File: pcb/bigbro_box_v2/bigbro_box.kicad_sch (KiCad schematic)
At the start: 42 parts, among them J1 Current Sense, J2 Display, J3 Mains, J4 Debug, J5 RFID, J6 Relay, J7 Ext, K1 G5LE-1, Q1 MMBT3904, Q2 MMBT3904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

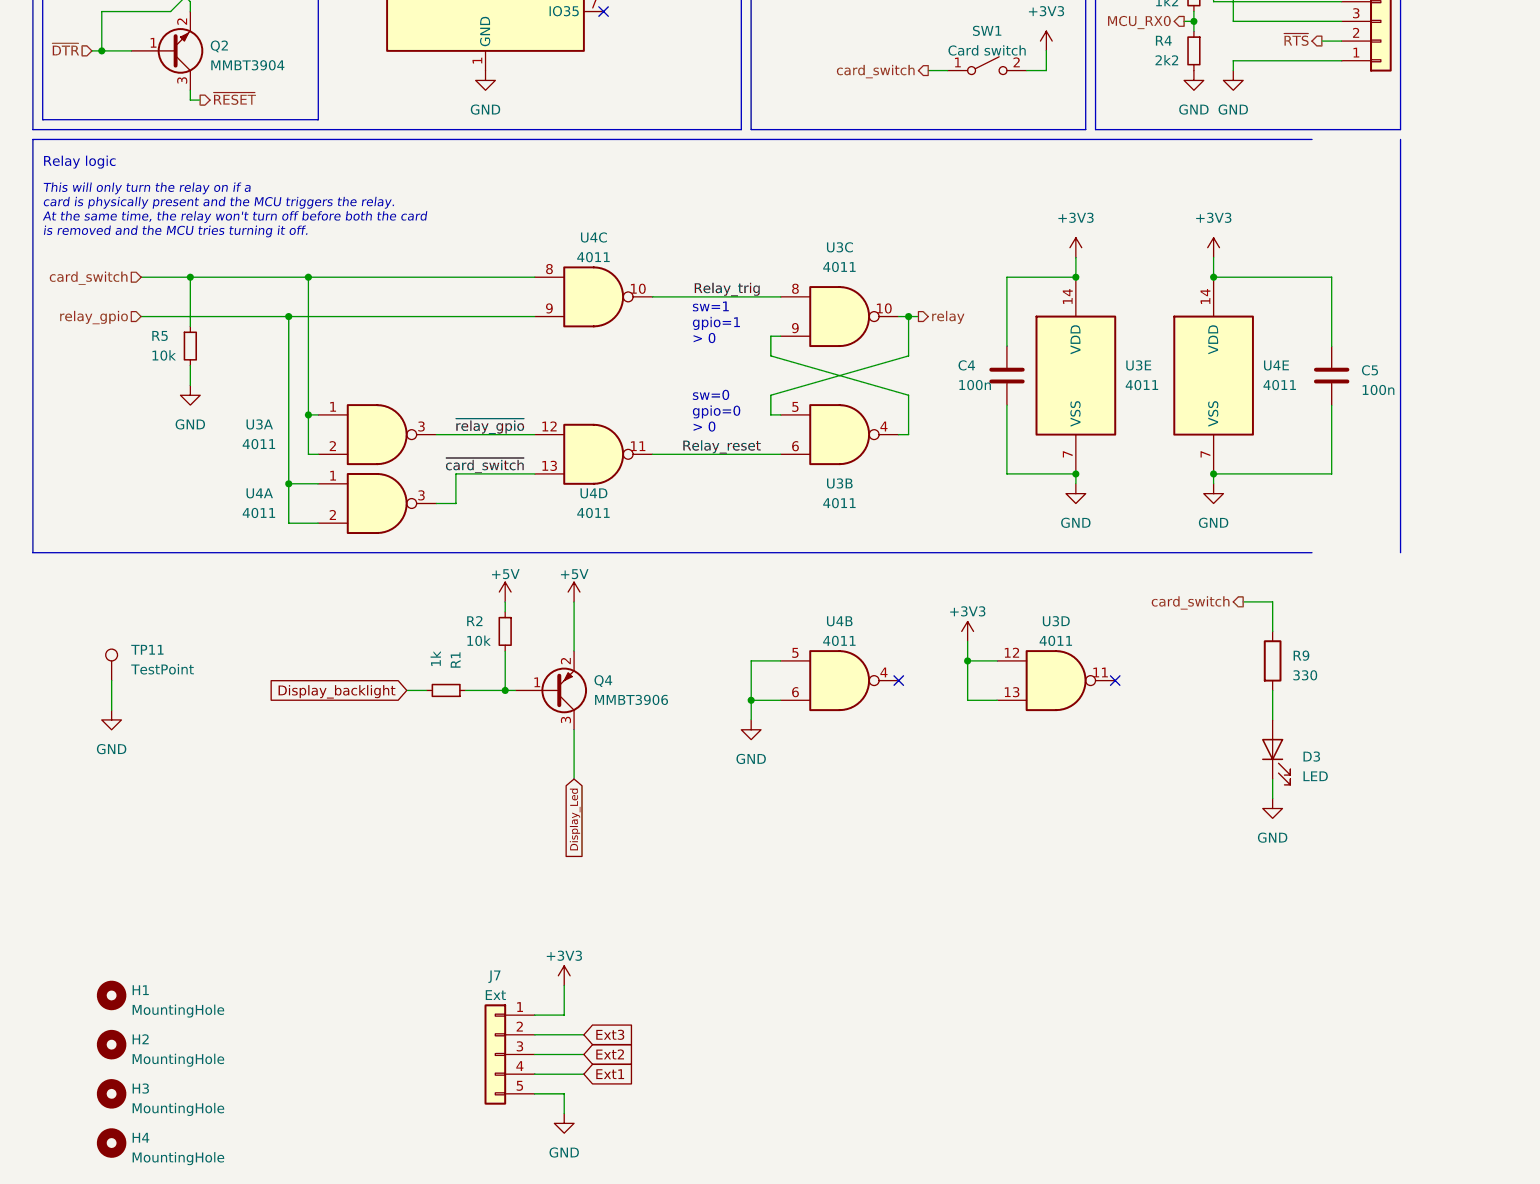
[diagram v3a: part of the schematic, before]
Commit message: Add reset and boot switches.
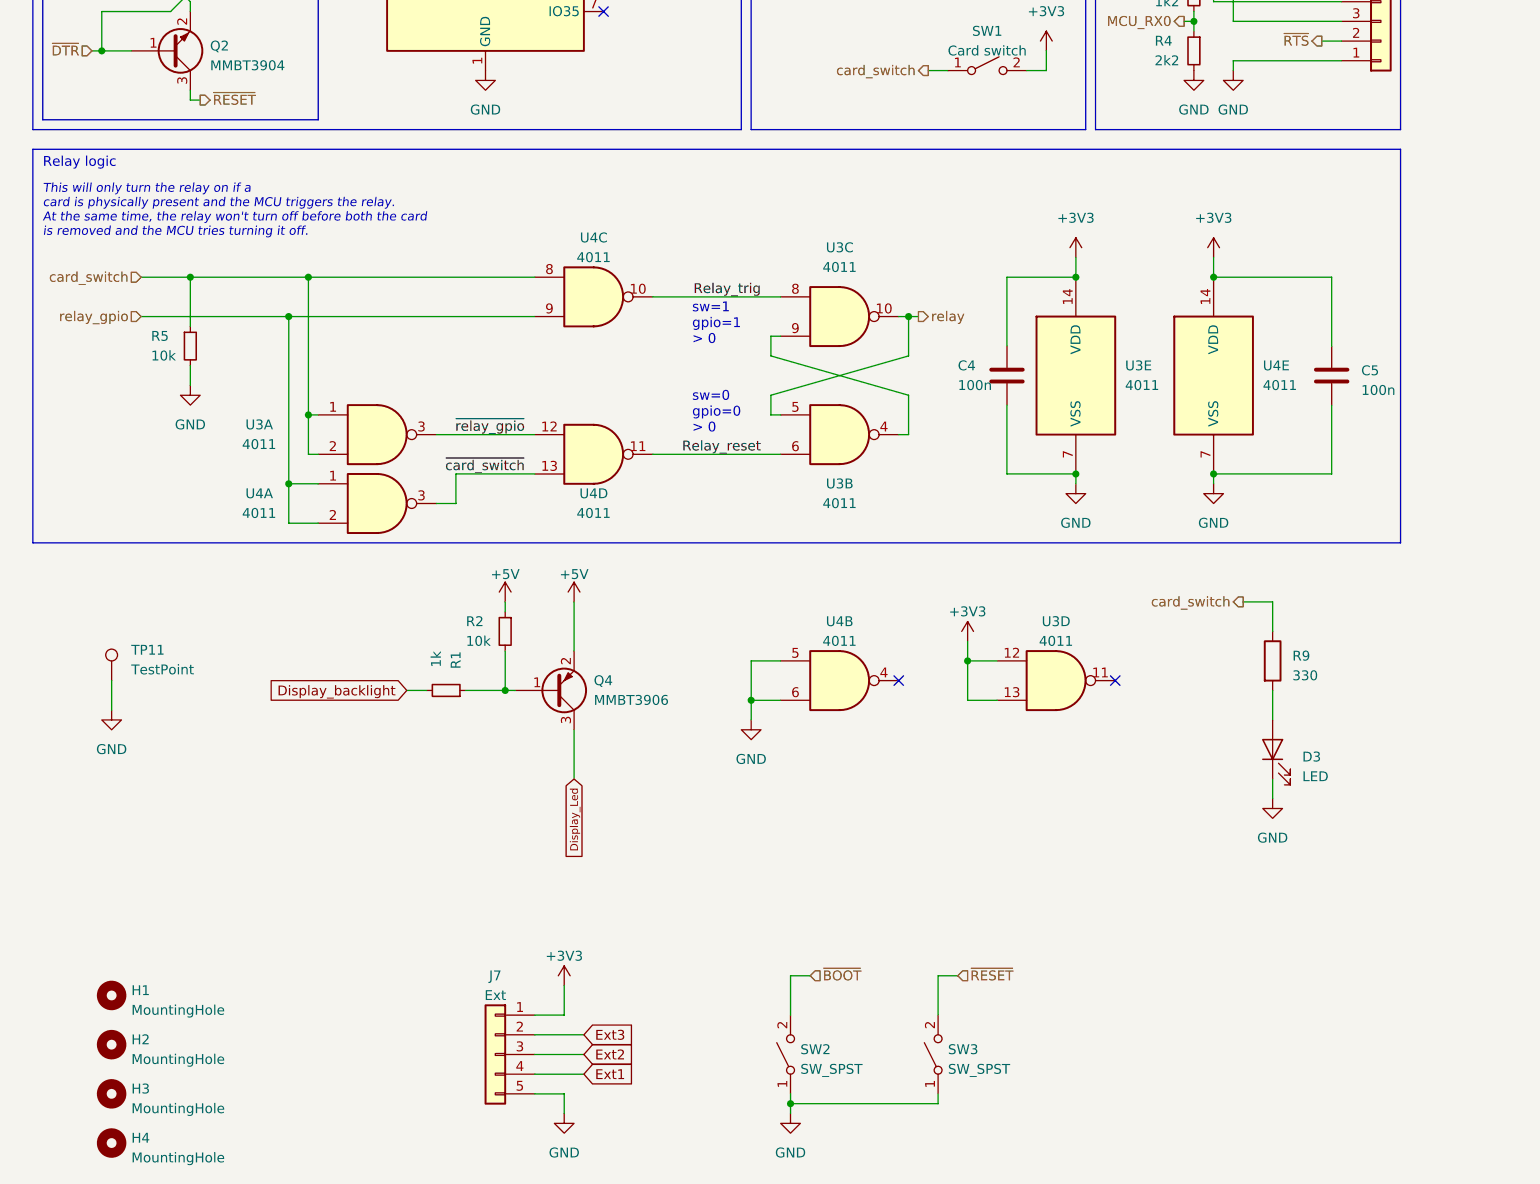
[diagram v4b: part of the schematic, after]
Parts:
- added SW2, SW3: SW_SPST, Button_Switch_SMD:SW_SPST_CK_RS282G05A3, symbol Switch:SW_SPST
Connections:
- net GND: now also SW2.1 (A), SW3.1 (A)
- net ~{BOOT}: now also SW2.2 (B)
- net ~{RESET}: now also SW3.2 (B)
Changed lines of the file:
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@@
   (junction (at 76.2 175.26) (diameter 0) (color 0 0 0 0)
+  )
+  (junction (at 113.03 228.6) (diameter 0) (color 0 0 0 0)
   )
   (junction (at 341.63 93.98) (diameter 0) (color 0 0 0 0)
@@
     (stroke (width 0) (type default))
   )
-  (polyline (pts (xy 15.24 104.14) (xy 15.24 157.48))
-    (stroke (width 0) (type default))
-  )
-  (polyline (pts (xy 15.24 104.14) (xy 180.34 104.14))
-    (stroke (width 0) (type default))
-  )
-  (polyline (pts (xy 15.24 157.48) (xy 180.34 157.48))
-    (stroke (width 0) (type default))
-  )
-  (polyline (pts (xy 191.77 157.48) (xy 191.77 104.14))
-    (stroke (width 0) (type default))
-  )
   (wire (pts (xy 88.9 69.85) (xy 93.98 69.85))
     (stroke (width 0) (type default))
@@
     (stroke (width 0) (type default))
   )
+  (wire (pts (xy 132.08 212.09) (xy 132.08 217.17))
+    (stroke (width 0) (type default))
+  )
   (wire (pts (xy 341.63 93.98) (xy 341.63 96.52))
     (stroke (width 0) (type default))
@@
     (stroke (width 0) (type default))
   )
+  (wire (pts (xy 113.03 212.09) (xy 113.03 217.17))
+    (stroke (width 0) (type default))
+  )
   (wire (pts (xy 35.56 83.82) (xy 35.56 85.09))
     (stroke (width 0) (type default))
@@
     (stroke (width 0) (type default))
   )
+  (wire (pts (xy 134.62 212.09) (xy 132.08 212.09))
+    (stroke (width 0) (type default))
+  )
   (wire (pts (xy 107.95 176.53) (xy 107.95 171.45))
     (stroke (width 0) (type default))
@@
     (stroke (width 0) (type default))
   )
+  (wire (pts (xy 132.08 227.33) (xy 132.08 228.6))
+    (stroke (width 0) (type default))
+  )
   (wire (pts (xy 135.89 171.45) (xy 139.7 171.45))
     (stroke (width 0) (type default))
@@
     (stroke (width 0) (type default))
   )
+  (wire (pts (xy 113.03 228.6) (xy 113.03 229.87))
+    (stroke (width 0) (type default))
+  )
   (wire (pts (xy 33.02 83.82) (xy 35.56 86.36))
     (stroke (width 0) (type default))
@@
     (stroke (width 0) (type default))
   )
+  (wire (pts (xy 132.08 228.6) (xy 113.03 228.6))
+    (stroke (width 0) (type default))
+  )
   (wire (pts (xy 179.07 52.07) (xy 179.07 57.15))
     (stroke (width 0) (type default))
@@
     (stroke (width 0) (type default))
   )
+  (wire (pts (xy 113.03 227.33) (xy 113.03 228.6))
+    (stroke (width 0) (type default))
+  )
   (wire (pts (xy 140.97 147.32) (xy 140.97 138.43))
     (stroke (width 0) (type default))
   )
+  (wire (pts (xy 115.57 212.09) (xy 113.03 212.09))
+    (stroke (width 0) (type default))
+  )
   (wire (pts (xy 85.09 163.83) (xy 85.09 170.18))
     (stroke (width 0) (type default))
@@
   (wire (pts (xy 149.86 147.32) (xy 140.97 147.32))
     (stroke (width 0) (type default))
+  )
+  (rectangle (start 15.24 105.41) (end 191.77 156.21)
+    (stroke (width 0) (type default))
+    (fill (type none))
   )
   (text "Power switching" (exclude_from_sim no)
@@
     (effects (font (size 1.27 1.27)) (justify right))
   )
+  (hierarchical_label "~{BOOT}" (shape input) (at 115.57 212.09 0) (fields_autoplaced)
+    (effects (font (size 1.27 1.27)) (justify left))
+  )
   (hierarchical_label "relay" (shape output) (at 129.54 127 0) (fields_autoplaced)
     (effects (font (size 1.27 1.27)) (justify left))
@@
   )
   (hierarchical_label "MCU_RX0" (shape input) (at 91.44 36.83 0) (fields_autoplaced)
+    (effects (font (size 1.27 1.27)) (justify left))
+  )
+  (hierarchical_label "~{RESET}" (shape input) (at 134.62 212.09 0) (fields_autoplaced)
     (effects (font (size 1.27 1.27)) (justify left))
   )
@@
     )
   )
+  (symbol (lib_id "power:GND") (at 113.03 229.87 0) (unit 1)
+    (in_bom yes) (on_board yes) (dnp no) (fields_autoplaced)
+    (property "Reference" "#PWR013" (at 113.03 236.22 0)
+      (effects (font (size 1.27 1.27)) hide)
+    )
+    (property "Value" "GND" (at 113.03 234.95 0)
+      (effects (font (size 1.27 1.27)))
+    )
+    (property "Footprint" "" (at 113.03 229.87 0)
+      (effects (font (size 1.27 1.27)) hide)
+    )
+    (property "Datasheet" "" (at 113.03 229.87 0)
+      (effects (font (size 1.27 1.27)) hide)
+    )
+    (pin "1")
+    (instances
+      (project "bigbro_box"
+        (path "/212a0d71-cc7b-49f8-b4ca-a935e5355dca"
+          (reference "#PWR013") (unit 1)
+        )
+      )
+    )
+  )
   (symbol (lib_id "Device:D_Small") (at 334.01 83.82 90) (mirror x) (unit 1)
     (in_bom yes) (on_board yes) (dnp no)
@@
         (path "/212a0d71-cc7b-49f8-b4ca-a935e5355dca"
           (reference "#PWR07") (unit 1)
+        )
+      )
+    )
+  )
+  (symbol (lib_id "Switch:SW_SPST") (at 132.08 222.25 90) (unit 1)
+    (in_bom yes) (on_board yes) (dnp no) (fields_autoplaced)
+    (property "Reference" "SW3" (at 133.35 221.615 90)
+      (effects (font (size 1.27 1.27)) (justify right))
+    )
+    (property "Value" "SW_SPST" (at 133.35 224.155 90)
+      (effects (font (size 1.27 1.27)) (justify right))
+    )
+    (property "Footprint" "Button_Switch_SMD:SW_SPST_CK_RS282G05A3" (at 132.08 222.25 0)
+      (effects (font (size 1.27 1.27)) hide)
+    )
+    (property "Datasheet" "~" (at 132.08 222.25 0)
+      (effects (font (size 1.27 1.27)) hide)
+    )
+    (pin "1")
+    (pin "2")
+    (instances
+      (project "bigbro_box"
+        (path "/212a0d71-cc7b-49f8-b4ca-a935e5355dca"
+          (reference "SW3") (unit 1)
         )
       )
@@
         )
       )
+    )
+  )
+  (symbol (lib_id "Switch:SW_SPST") (at 113.03 222.25 90) (unit 1)
+    (in_bom yes) (on_board yes) (dnp no) (fields_autoplaced)
+    (property "Reference" "SW2" (at 114.3 221.615 90)
+      (effects (font (size 1.27 1.27)) (justify right))
+    )
+    (property "Value" "SW_SPST" (at 114.3 224.155 90)
+      (effects (font (size 1.27 1.27)) (justify right))
+    )
+    (property "Footprint" "Button_Switch_SMD:SW_SPST_CK_RS282G05A3" (at 113.03 222.25 0)
+      (effects (font (size 1.27 1.27)) hide)
+    )
+    (property "Datasheet" "~" (at 113.03 222.25 0)
+      (effects (font (size 1.27 1.27)) hide)
+    )
+    (pin "1")
+    (pin "2")
+    (instances
+      (project "bigbro_box"
+        (path "/212a0d71-cc7b-49f8-b4ca-a935e5355dca"
+          (reference "SW2") (unit 1)
+        )
+      )

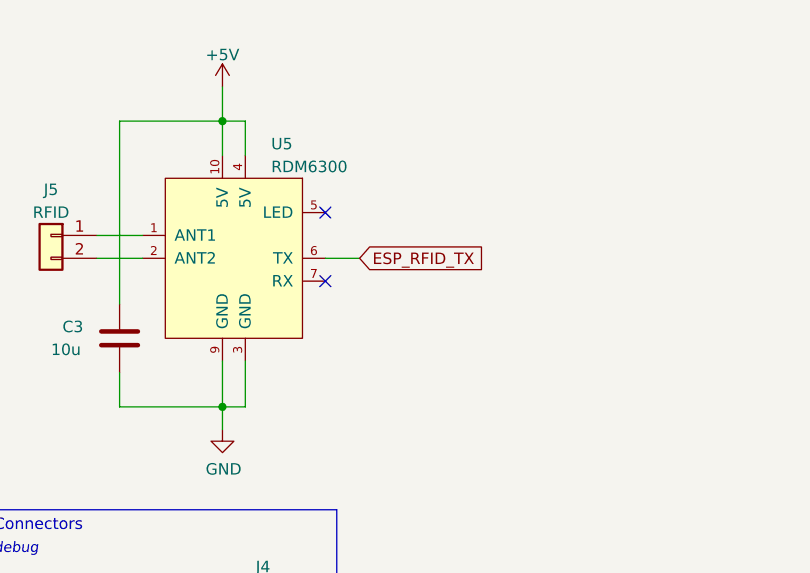
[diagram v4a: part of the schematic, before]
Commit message: Add voltage divider for RFID.
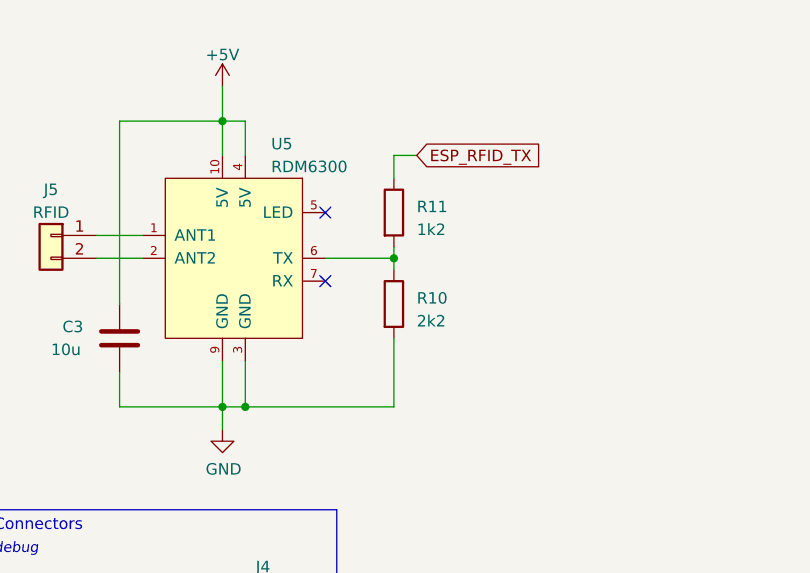
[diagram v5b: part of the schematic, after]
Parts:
- added R10: 2k2, Resistor_SMD:R_0603_1608Metric, symbol Device:R
- added R11: 1k2, Resistor_SMD:R_0603_1608Metric, symbol Device:R
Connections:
- net ESP_RFID_TX: now also R11.1; no longer U5.6 (TX)
- net GND: now also R10.2
- new net: R10.1, R11.2, U5.6 (TX)
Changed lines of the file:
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@@
   (junction (at 48.26 148.59) (diameter 0) (color 0 0 0 0)
   )
+  (junction (at 181.61 57.15) (diameter 0) (color 0 0 0 0)
+  )
   (junction (at 76.2 175.26) (diameter 0) (color 0 0 0 0)
   )
@@
   )
   (junction (at 24.13 92.71) (diameter 0) (color 0 0 0 0)
+  )
+  (junction (at 198.12 40.64) (diameter 0) (color 0 0 0 0)
   )
   (junction (at 35.56 121.92) (diameter 0) (color 0 0 0 0)
@@
     (stroke (width 0) (type default))
   )
-  (wire (pts (xy 190.5 40.64) (xy 194.31 40.64))
+  (wire (pts (xy 190.5 40.64) (xy 198.12 40.64))
     (stroke (width 0) (type default))
   )
@@
     (stroke (width 0) (type default))
   )
+  (wire (pts (xy 198.12 40.64) (xy 198.12 39.37))
+    (stroke (width 0) (type default))
+  )
   (wire (pts (xy 55.88 29.21) (xy 58.42 29.21))
     (stroke (width 0) (type default))
@@
     (stroke (width 0) (type default))
   )
+  (wire (pts (xy 198.12 29.21) (xy 198.12 31.75))
+    (stroke (width 0) (type default))
+  )
   (wire (pts (xy 165.1 40.64) (xy 170.18 40.64))
     (stroke (width 0) (type default))
@@
     (stroke (width 0) (type default))
   )
+  (wire (pts (xy 198.12 40.64) (xy 198.12 41.91))
+    (stroke (width 0) (type default))
+  )
   (wire (pts (xy 25.4 173.99) (xy 25.4 177.8))
     (stroke (width 0) (type default))
@@
     (stroke (width 0) (type default))
   )
+  (wire (pts (xy 198.12 57.15) (xy 198.12 49.53))
+    (stroke (width 0) (type default))
+  )
   (wire (pts (xy 134.62 212.09) (xy 132.08 212.09))
     (stroke (width 0) (type default))
@@
     (stroke (width 0) (type default))
   )
+  (wire (pts (xy 181.61 57.15) (xy 198.12 57.15))
+    (stroke (width 0) (type default))
+  )
   (wire (pts (xy 323.85 73.66) (xy 323.85 74.93))
     (stroke (width 0) (type default))
@@
   )
   (wire (pts (xy 76.2 175.26) (xy 77.47 175.26))
+    (stroke (width 0) (type default))
+  )
+  (wire (pts (xy 200.66 29.21) (xy 198.12 29.21))
     (stroke (width 0) (type default))
   )
@@
     )
   )
-  (global_label "ESP_RFID_TX" (shape input) (at 194.31 40.64 0) (fields_autoplaced)
+  (global_label "ESP_RFID_TX" (shape input) (at 200.66 29.21 0) (fields_autoplaced)
     (effects (font (size 1.27 1.27)) (justify left))
-    (property "Intersheetrefs" "${INTERSHEET_REFS}" (at 208.6974 40.5606 0)
+    (property "Intersheetrefs" "${INTERSHEET_REFS}" (at 215.0474 29.1306 0)
       (effects (font (size 1.27 1.27)) (justify left) hide)
     )
@@
         (path "/212a0d71-cc7b-49f8-b4ca-a935e5355dca"
           (reference "#PWR0107") (unit 1)
+        )
+      )
+    )
+  )
+  (symbol (lib_id "Device:R") (at 198.12 45.72 0) (unit 1)
+    (in_bom yes) (on_board yes) (dnp no) (fields_autoplaced)
+    (property "Reference" "R10" (at 200.66 45.085 0)
+      (effects (font (size 1.27 1.27)) (justify left))
+    )
+    (property "Value" "2k2" (at 200.66 47.625 0)
+      (effects (font (size 1.27 1.27)) (justify left))
+    )
+    (property "Footprint" "Resistor_SMD:R_0603_1608Metric" (at 196.342 45.72 90)
+      (effects (font (size 1.27 1.27)) hide)
+    )
+    (property "Datasheet" "~" (at 198.12 45.72 0)
+      (effects (font (size 1.27 1.27)) hide)
+    )
+    (pin "1")
+    (pin "2")
+    (instances
+      (project "bigbro_box"
+        (path "/212a0d71-cc7b-49f8-b4ca-a935e5355dca"
+          (reference "R10") (unit 1)
         )
       )
@@
         )
       )
+    )
+  )
+  (symbol (lib_id "Device:R") (at 198.12 35.56 0) (unit 1)
+    (in_bom yes) (on_board yes) (dnp no) (fields_autoplaced)
+    (property "Reference" "R11" (at 200.66 34.925 0)
+      (effects (font (size 1.27 1.27)) (justify left))
+    )
+    (property "Value" "1k2" (at 200.66 37.465 0)
+      (effects (font (size 1.27 1.27)) (justify left))
+    )
+    (property "Footprint" "Resistor_SMD:R_0603_1608Metric" (at 196.342 35.56 90)
+      (effects (font (size 1.27 1.27)) hide)
+    )
+    (property "Datasheet" "~" (at 198.12 35.56 0)
+      (effects (font (size 1.27 1.27)) hide)
+    )
+    (pin "1")
+    (pin "2")
+    (instances
+      (project "bigbro_box"
+        (path "/212a0d71-cc7b-49f8-b4ca-a935e5355dca"
+          (reference "R11") (unit 1)
+        )
+      )

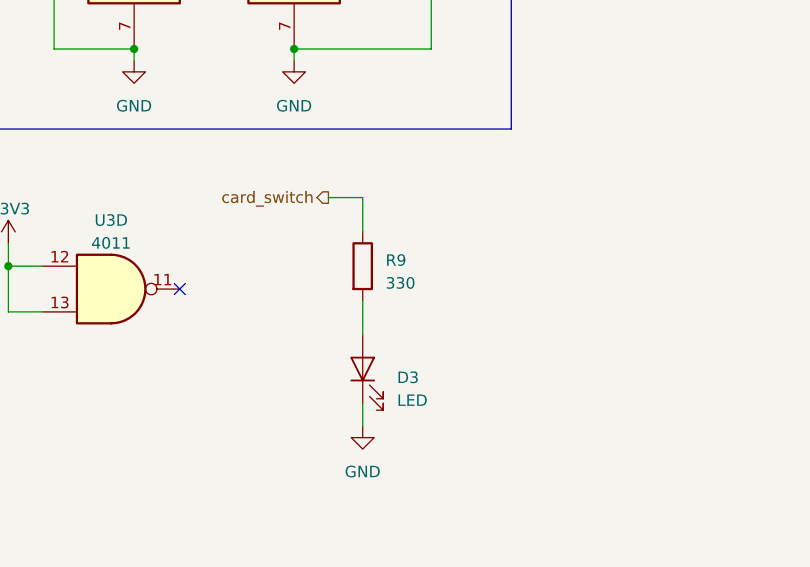
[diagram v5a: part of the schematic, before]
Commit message: Increase value of switch LED resistor.
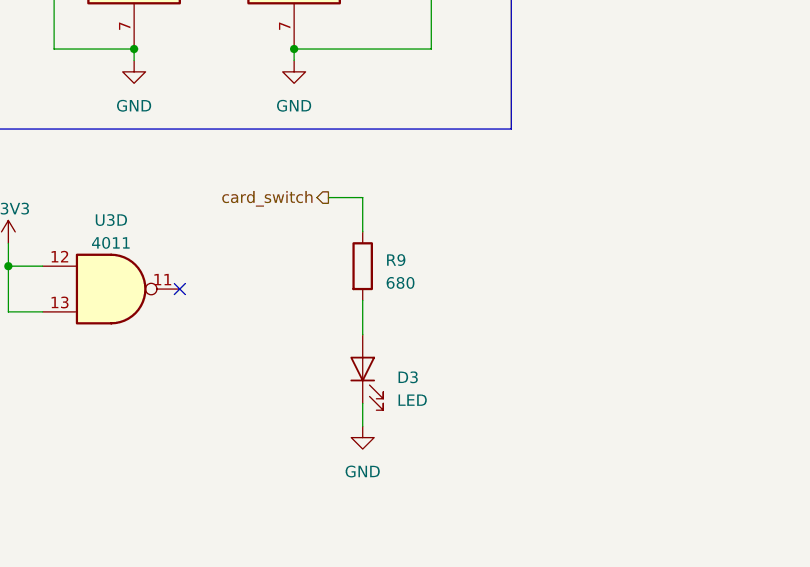
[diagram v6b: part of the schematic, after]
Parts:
- R9: value 330 -> 680
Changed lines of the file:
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@@
       (effects (font (size 1.27 1.27)) (justify left))
     )
-    (property "Value" "330" (at 177.8 173.355 0)
+    (property "Value" "680" (at 177.8 173.355 0)
       (effects (font (size 1.27 1.27)) (justify left))
     )
